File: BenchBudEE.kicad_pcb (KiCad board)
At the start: 4 copper layers, 165.1 x 63.5 mm, 143 parts, among them K1 1461069-5, P1 24-pin Mini-Fit Jr., P2 CONN_2, P3 CONN_3X2, P4 12-pin Terminal Block, P5 3-pin TB, P6 CONN_1, P7 CONN_1, Q1 2N3404, Q2 DMN65D8L-7, Q3 AOD476, Q4 AOD476, SW1 Power Switch, U1 LTV-816S, U10 LMT84, U11 OPA4170, U2 AP5726, U3 LM317T, U4 LM317T, U5 LM337T, U6 LM337T, U8 MCP4801, U9 MCP3901

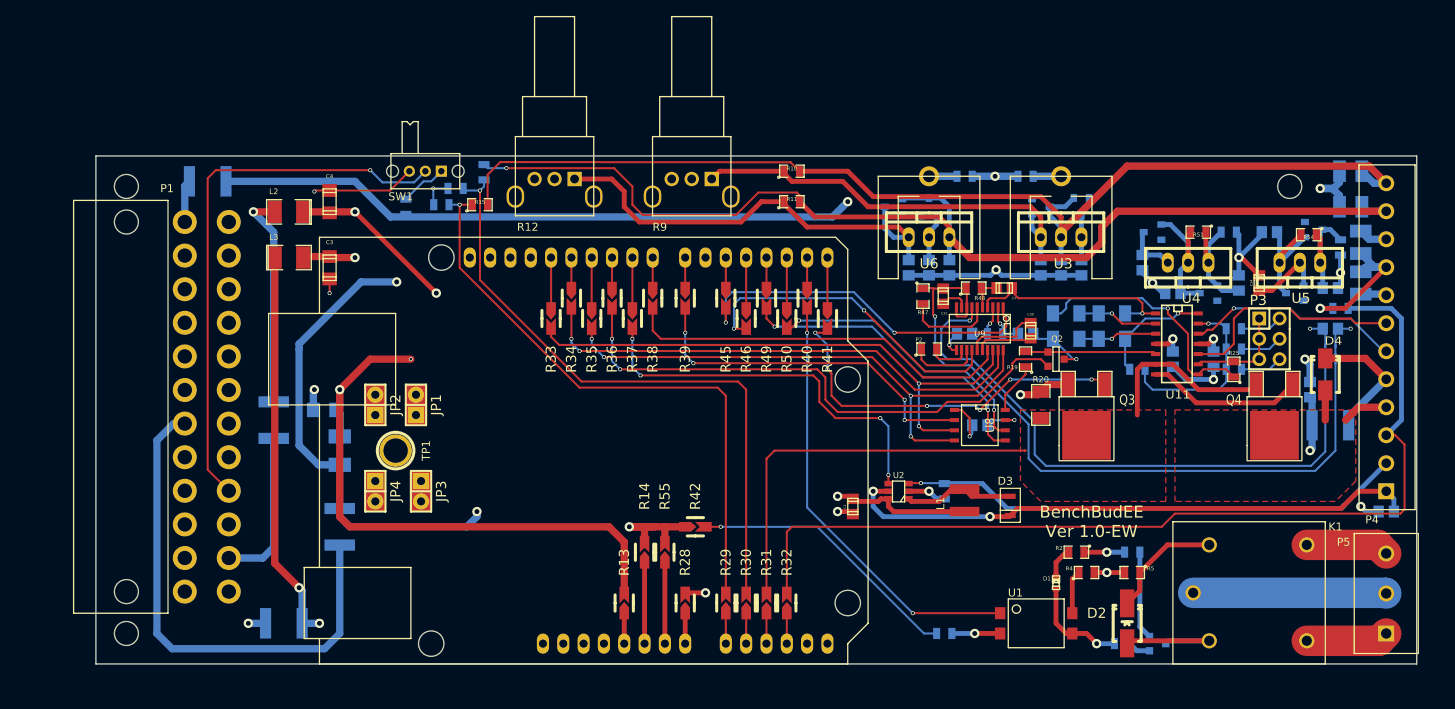
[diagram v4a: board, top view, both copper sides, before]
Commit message: Test points added, silk screen updates
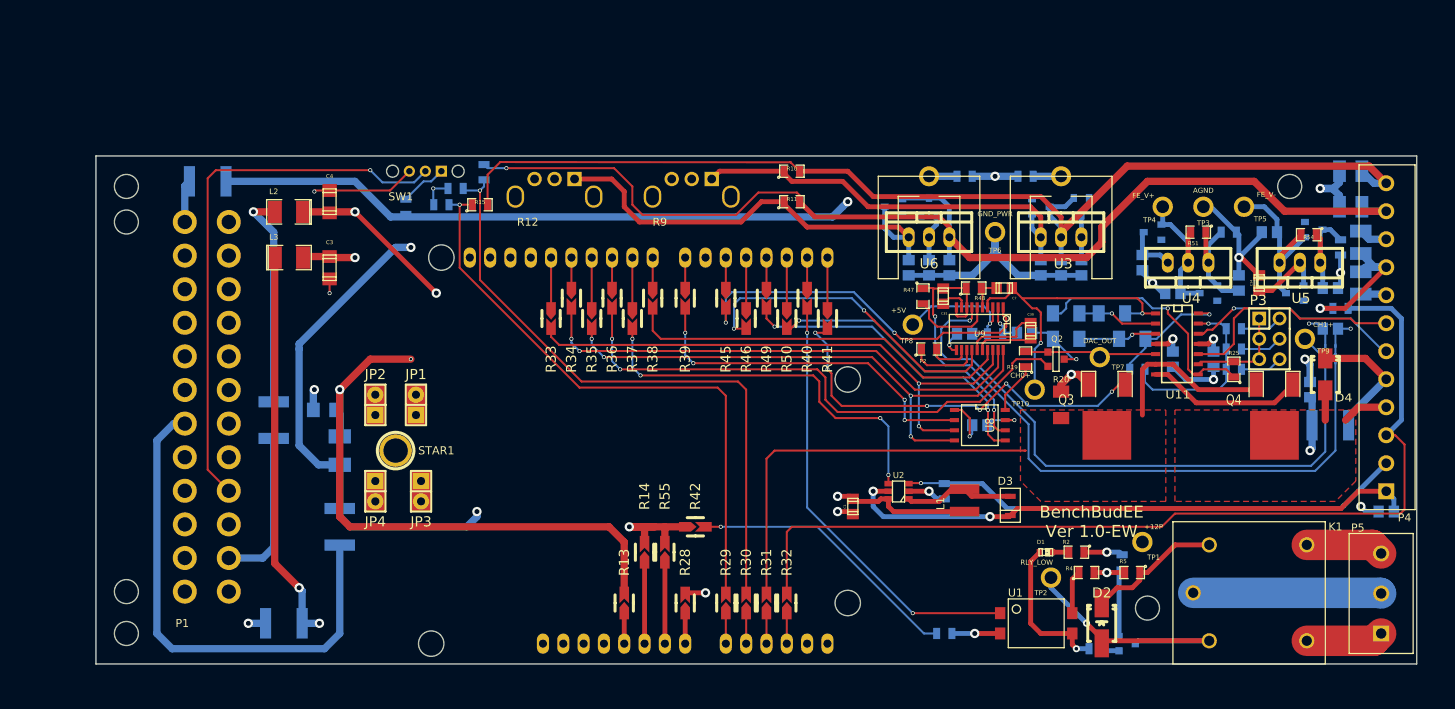
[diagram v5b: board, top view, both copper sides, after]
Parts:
- added 3 mm: VAL**, BenchBudEE:3mm-NPTH, F.Cu at (202.6, 107.3)
- added STAR1: CONN_1, Connect:1pin, F.Cu at (108.6, 87.6)
- added TP10: CH0+, BenchBudEE:TestPointTH, F.Cu at (188.5, 80.0)
- added TP2: RLY_LOW, BenchBudEE:TestPointTH, F.Cu at (190.5, 103.5)
- added TP3: AGND, BenchBudEE:TestPointTH, F.Cu at (209.6, 57.1)
- added TP4: FE_V+, BenchBudEE:TestPointTH, F.Cu at (204.5, 57.1)
- added TP5: FE_V-, BenchBudEE:TestPointTH, F.Cu at (214.6, 57.1)
- added TP6: GND_PWR, BenchBudEE:TestPointTH, F.Cu at (183.5, 60.3)
- added TP7: DAC_OUT, BenchBudEE:TestPointTH, F.Cu at (196.6, 75.9)
- added TP8: +5V, BenchBudEE:TestPointTH, F.Cu at (173.2, 71.9)
- added TP9: CH1+, BenchBudEE:TestPointTH, F.Cu at (222.2, 73.7)
- Q3, Q4: footprint SMD_Packages:DPAK2 -> BenchBudEE:DPAK2_BB
- R20: footprint SMD_Packages:SM1206 -> BenchBudEE:SM1206_BB
- TP1: value CONN_1 -> +12P; footprint Connect:1pin -> BenchBudEE:TestPointTH
- moved TP1 94.0 mm to (201.9, 99.1)
- moved D1 4.02 mm to (189.9, 100.3), turned to 0 degrees
- moved Q1 3.81 mm to (200.0, 111.8)
- moved R3 3.24 mm to (196.2, 112.4)
- moved D2 3.18 mm to (196.8, 109.2)
- moved Q3 2.54 mm to (197.5, 79.4)
- moved R20 2.54 mm to (191.8, 81.9)
- moved R24 2.54 mm to (200.7, 73.7)
- moved R6 1.80 mm to (199.4, 101.6), turned to 270 degrees
- moved P5 0.63 mm to (231.8, 110.5)
- moved C5 0.18 mm to (187.2, 72.9)
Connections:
- TP1 pad 1: GND -> +12P
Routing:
- net Net-(D2-Pad1): track 16.0 -> 33.8 mm, vias 0 -> 1
- net /Thermocouple/CH0+: track 27.3 -> 40.5 mm, vias 1 -> 2
- net +5V: track 94.4 -> 107.1 mm
- net GND_PWR: track 59.4 -> 66.2 mm, vias 5 -> 4
- net +3.3V: track 155.5 -> 161.9 mm
- net FE_V-: track 34.3 -> 40.6 mm
- net Net-(D1-Pad1): track 12.7 -> 18.8 mm
- net +5P: track 218.1 -> 223.4 mm
- net AGND: track 153.3 -> 157.8 mm
- net /Arduino/FAN_MODE: track 47.2 -> 51.5 mm
- net /Thermocouple/CH1+: track 76.9 -> 80.9 mm
- net /PowerAdjustmentMonitor/V-_ADJ: track 142.3 -> 145.4 mm
- net Net-(Q1-Pad1): track 11.0 -> 8.48 mm
- net Net-(D2-Pad2): track 14.6 -> 17.0 mm
- net FE_V+: track 31.7 -> 34.0 mm
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
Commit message: Added some R/C to analog sections
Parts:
- removed TP4: FE_V+, BenchBudEE:TestPointTH
- removed TP5: FE_V-, BenchBudEE:TestPointTH
- added C32: C, Capacitors_SMD:c_0805, F.Cu at (205.7, 80.5)
- added C33: C, Capacitors_SMD:c_0805, B.Cu at (229.2, 82.5)
- added K2: CONN_3, Pin_Headers:Pin_Header_Straight_1x03, F.Cu at (214.6, 56.5)
- added K3: CONN_3, Pin_Headers:Pin_Header_Straight_1x03, F.Cu at (202.6, 56.5)
- added R59: 0, SMD_Packages:SM0805, F.Cu at (193.8, 75.4)
- added R60: 0, SMD_Packages:SM0805, F.Cu at (210.1, 80.5)
- added R61: 0, SMD_Packages:SM0805, F.Cu at (202.2, 80.5)
- added R62: 1k, SMD_Packages:SM0805, F.Cu at (227.1, 73.9)
- added R63: 0, SMD_Packages:SM0805, B.Cu at (188.0, 70.1)
- added R64: 1k, SMD_Packages:SM0805, F.Cu at (227.1, 76.2)
- C14, R48, R54: moved to B.Cu
- moved C12 17.1 mm to (207.1, 86.6)
- moved C14 13.3 mm to (212.7, 54.0), turned to 180 degrees
- moved C16 10.6 mm to (205.1, 54.0), turned to 180 degrees
- moved R48 5.80 mm to (185.9, 70.1), turned to 270 degrees
- moved D9 4.92 mm to (218.4, 60.3), turned to 180 degrees
- moved TH5 4.49 mm to (226.1, 88.9), turned to 90 degrees
- moved C22 4.02 mm to (216.5, 64.1), turned to 90 degrees
- moved R47 3.10 mm to (176.3, 70.9)
- moved U10 2.42 mm to (227.8, 75.4)
- moved C7 2.34 mm to (182.4, 67.8)
- moved D4 2.29 mm to (226.7, 79.4), turned to 0 degrees
- moved C10 1.65 mm to (227.1, 72.4)
- moved 3 mm 1.27 mm to (221.6, 54.6)
- moved C30 1.02 mm to (186.9, 72.6)
- moved R54 0.97 mm to (222.9, 61.6)
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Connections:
- C31 pad 2: AGND -> Net-(C31-Pad2)
- D5 pad 1: -12V -> Net-(D5-Pad1)
- D6 pad 2: +12V -> Net-(D6-Pad2)
- P4 pad 6: /TerminalBlock/TC_IN- -> /TerminalBlock/TC_IN+
- P4 pad 7: /TerminalBlock/TC_IN+ -> /TerminalBlock/TC_IN-
- Q2 pad 3: AGND -> Net-(Q2-Pad3)
- R22 pad 1: AGND -> Net-(R22-Pad1)
- R48 pad 1: AGND -> Net-(R22-Pad1)
- U10 pad 3: /Thermocouple/CH1+ -> Net-(R64-Pad2)
- U11 pad 10: /TerminalBlock/TC_IN+ -> /TerminalBlock/TC_IN-
- U11 pad 12: /TerminalBlock/TC_IN- -> /TerminalBlock/TC_IN+
- U11 pad 6: /Arduino/CURR_MEAS -> Net-(C32-Pad2)
- U11 pad 7: Net-(Q4-Pad1) -> Net-(C32-Pad1)
- U4 pad 3: +12V -> Net-(D6-Pad2)
- U5 pad 2: -12V -> Net-(D5-Pad1)
- U9 pad 10: AGND -> Net-(C31-Pad2)
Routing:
- net AGND: track 157.8 -> 83.3 mm
- net Net-(D6-Pad2): track 0.00 -> 20.4 mm
- net Net-(D5-Pad1): track 0.00 -> 12.5 mm
- net -12V: track 223.9 -> 213.3 mm
- net Net-(Q4-Pad1): track 19.6 -> 10.2 mm, vias 0 -> 2
- net Net-(R22-Pad1): track 0.00 -> 8.69 mm
- net Net-(C32-Pad1): track 0.00 -> 7.31 mm
- net Net-(C32-Pad2): track 0.00 -> 6.90 mm
- net /Arduino/CURR_MEAS: track 71.4 -> 65.3 mm
- net Net-(C31-Pad2): track 0.00 -> 3.66 mm
- net /Thermocouple/CH1+: track 80.9 -> 77.3 mm
- net /Thermocouple/CH1-: track 10.6 -> 7.15 mm
- net +12V: track 223.1 -> 219.8 mm
- net Net-(R64-Pad2): track 0.00 -> 3.14 mm, vias 0 -> 1
- net /Thermocouple/CH0-: track 4.38 -> 7.43 mm, vias 0 -> 1
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
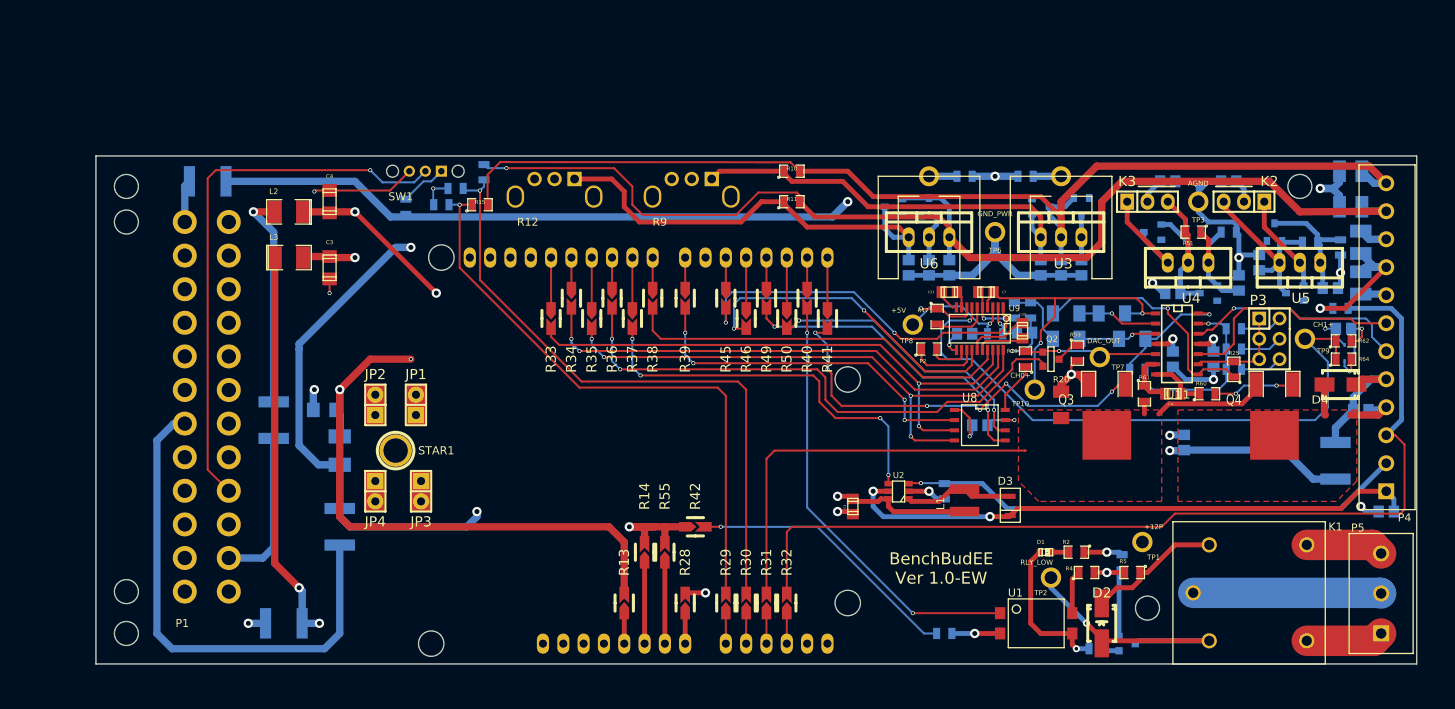
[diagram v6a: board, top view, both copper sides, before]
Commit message: Via annular ring size fixed
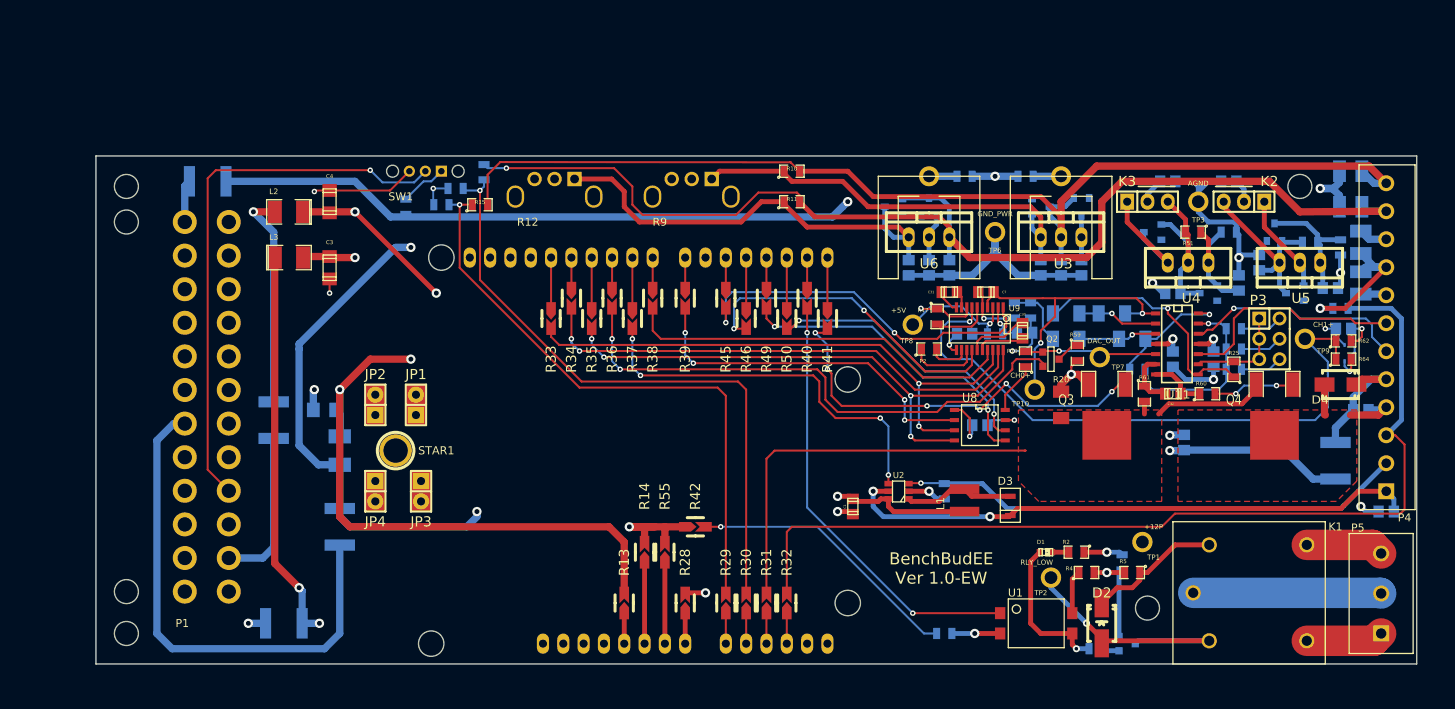
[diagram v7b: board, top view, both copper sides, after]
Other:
- rule via_min_size: 0.508 -> 0.6858

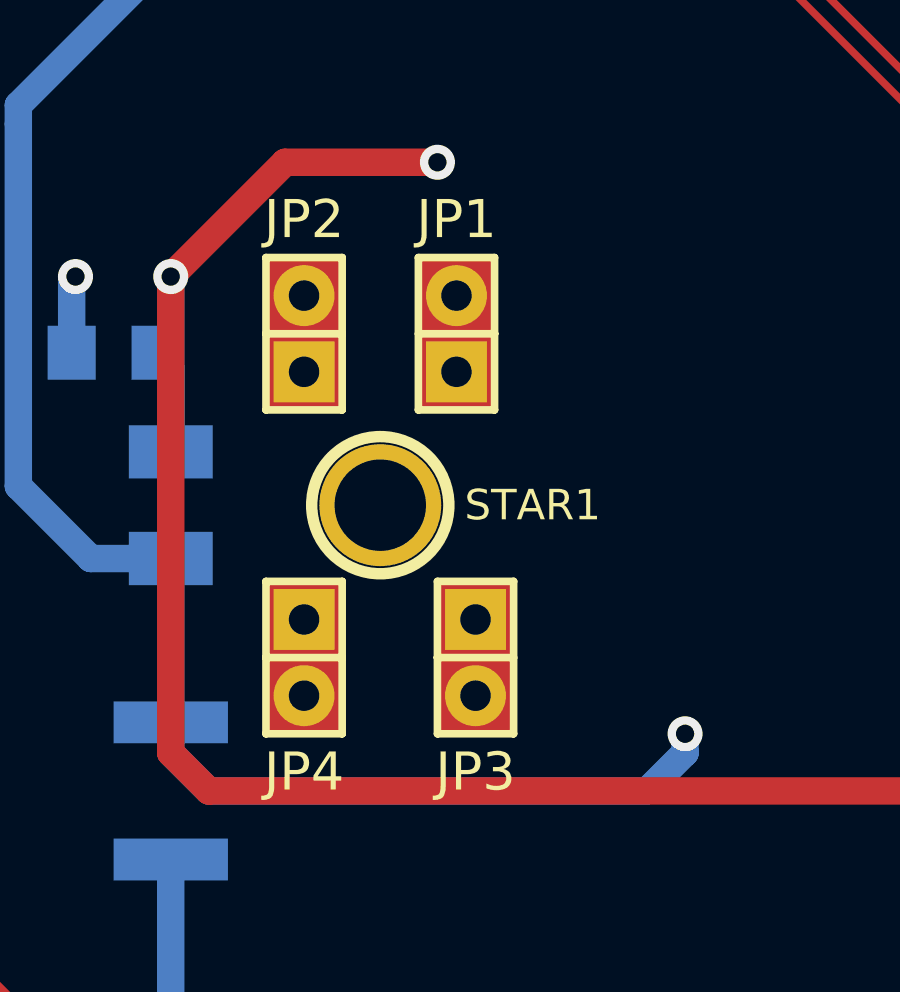
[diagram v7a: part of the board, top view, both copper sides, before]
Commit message: Ground point tweaked a bit
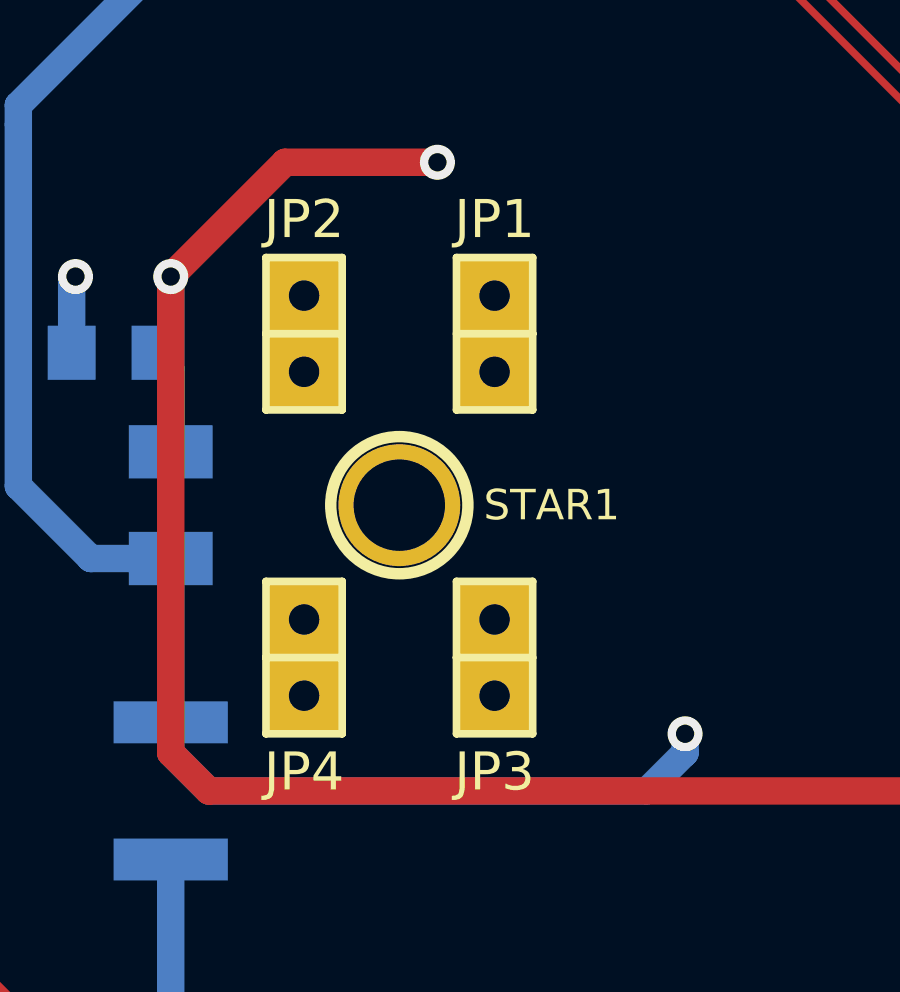
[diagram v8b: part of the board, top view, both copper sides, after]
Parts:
- moved JP1 1.27 mm to (112.4, 81.9)
- moved STAR1 0.64 mm to (109.2, 87.6)
- moved JP3 0.63 mm to (112.4, 92.7)
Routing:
- net GND: track 70.7 -> 70.0 mm
